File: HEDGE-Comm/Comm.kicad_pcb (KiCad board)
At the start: 2 copper layers, 90.2 x 95.9 mm, 6 parts

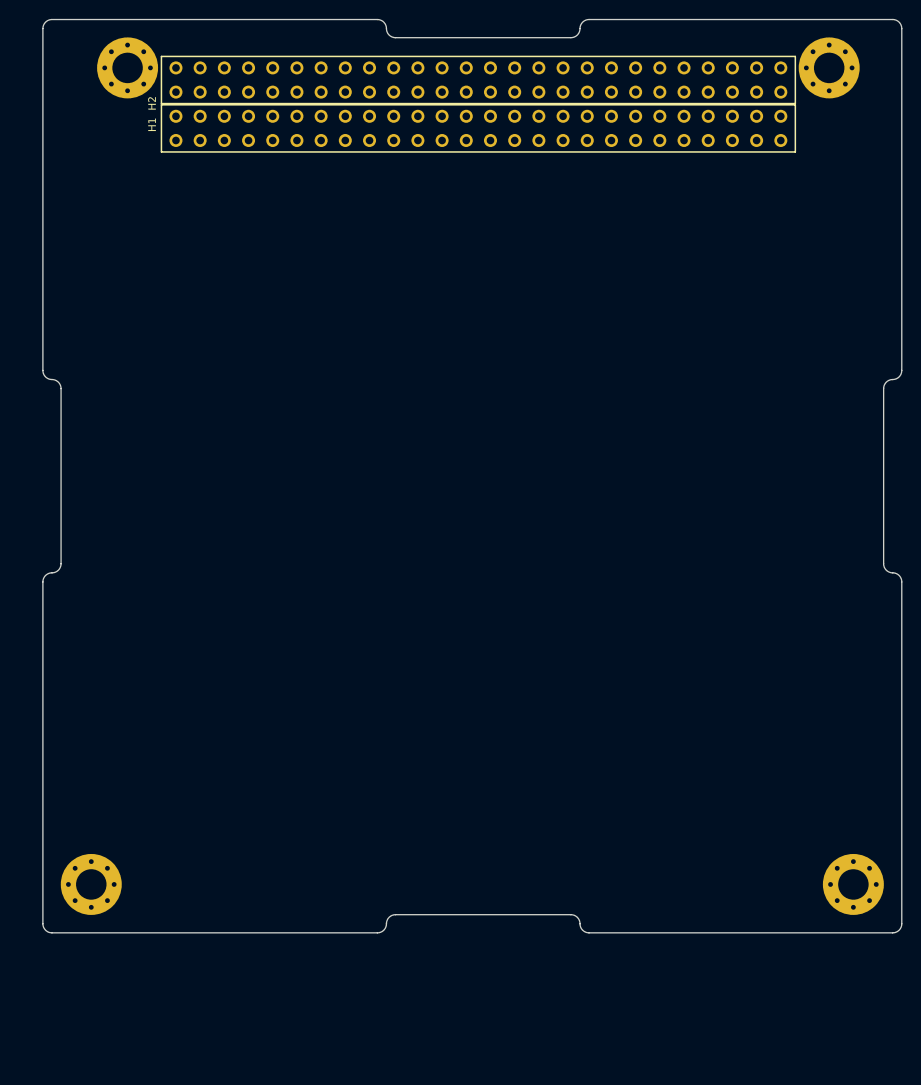
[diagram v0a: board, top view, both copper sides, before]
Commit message: Refactor Data PCB files; enter RS485; enter Iridium radio power
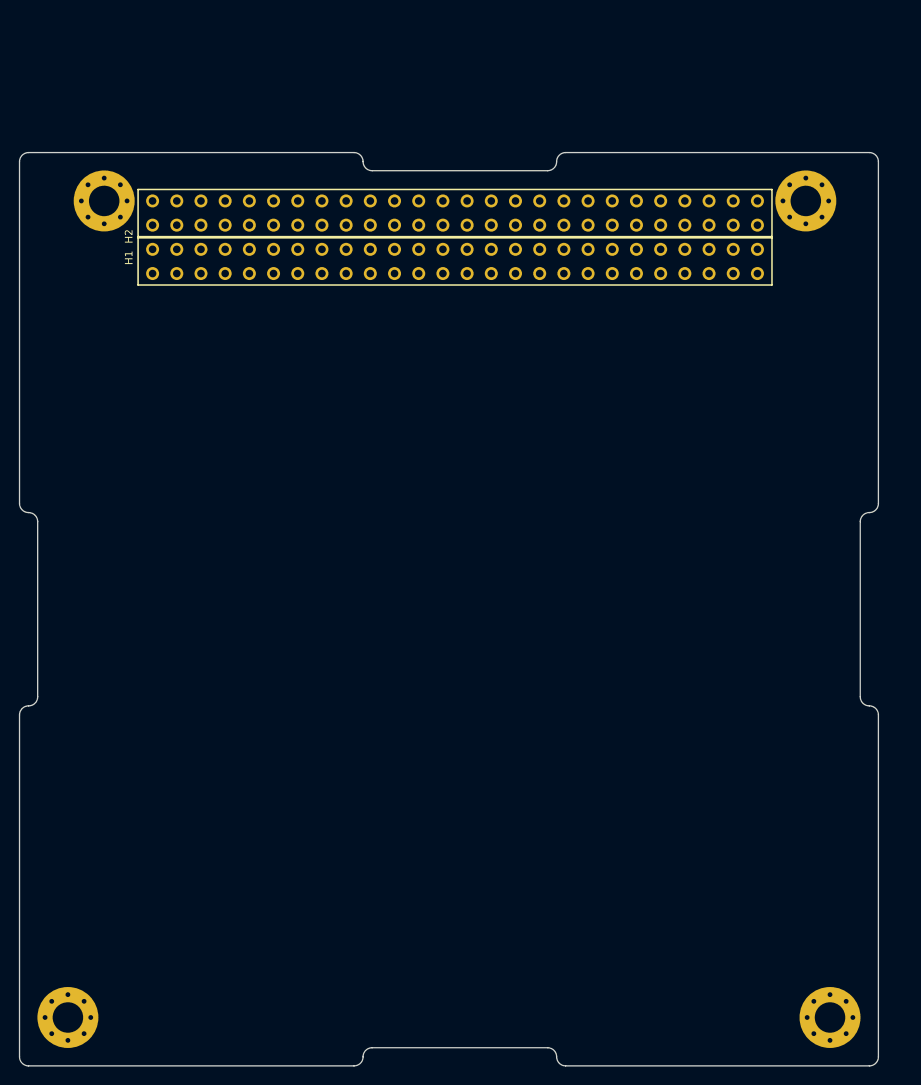
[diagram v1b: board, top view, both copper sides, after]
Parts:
- moved MH3 14.2 mm to (189.9, 148.4)
- moved MH4 14.2 mm to (109.9, 148.4)
- moved H1 14.2 mm to (118.8, 70.3)
- moved H2 14.2 mm to (118.8, 65.2)
- moved MH1 14.2 mm to (113.7, 62.6)
- moved MH2 14.2 mm to (187.3, 62.6)
